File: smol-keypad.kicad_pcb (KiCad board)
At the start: 2 copper layers, 78.6 x 99.2 mm, 34 parts, among them SW1 SW_PUSH, U1 ProMicro

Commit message: test
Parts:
- moved D16 65.4 mm to (102.4, 127.0), turned to 0 degrees
- moved D4 64.0 mm to (159.5, 127.0), turned to 0 degrees
- moved MX13 58.7 mm to (102.4, 61.9), turned to 270 degrees
- moved MX1 57.2 mm to (159.5, 61.9), turned to 270 degrees
- moved MX16 57.2 mm to (102.4, 119.1), turned to 270 degrees
- moved MX4 55.6 mm to (159.5, 119.1), turned to 270 degrees
- moved D12 52.6 mm to (121.5, 127.0), turned to 0 degrees
- moved D8 52.0 mm to (140.5, 127.0), turned to 0 degrees
- moved D13 51.4 mm to (102.4, 69.8), turned to 0 degrees
- moved D1 49.6 mm to (159.5, 69.8), turned to 0 degrees
- moved D15 47.8 mm to (102.4, 108.0), turned to 0 degrees
- moved D3 45.8 mm to (159.5, 108.0), turned to 0 degrees
- moved MX14 44.0 mm to (102.4, 81.0), turned to 270 degrees
- moved MX9 44.0 mm to (121.4, 61.9), turned to 270 degrees
- moved MX15 43.3 mm to (102.4, 100.0), turned to 270 degrees
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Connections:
- U1 pad 10: Net-(U1-Pad10) -> /row1
- U1 pad 11: Net-(U1-Pad11) -> /row2
- U1 pad 12: Net-(U1-Pad12) -> /row3
- U1 pad 5: Net-(U1-Pad5) -> /col3
- U1 pad 6: Net-(U1-Pad6) -> /col2
- U1 pad 7: Net-(U1-Pad7) -> /col1
- U1 pad 8: Net-(U1-Pad8) -> /col0
- U1 pad 9: Net-(U1-Pad9) -> /row0
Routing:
- net /col3: track 57.1 -> 139.7 mm
- net /col2: track 57.1 -> 122.5 mm
- net /col1: track 57.1 -> 103.5 mm
- net /row3: track 58.8 -> 102.8 mm
- net GND: track 0.00 -> 40.7 mm
- net Net-(SW1-Pad1): track 0.00 -> 36.6 mm
- net /row0: track 58.8 -> 89.3 mm
- net /row2: track 58.9 -> 87.2 mm
- net /col0: track 57.1 -> 85.4 mm
- net /row1: track 58.8 -> 81.3 mm
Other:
- board size 78.6 x 99.2 mm -> 79.4 x 103.2 mm

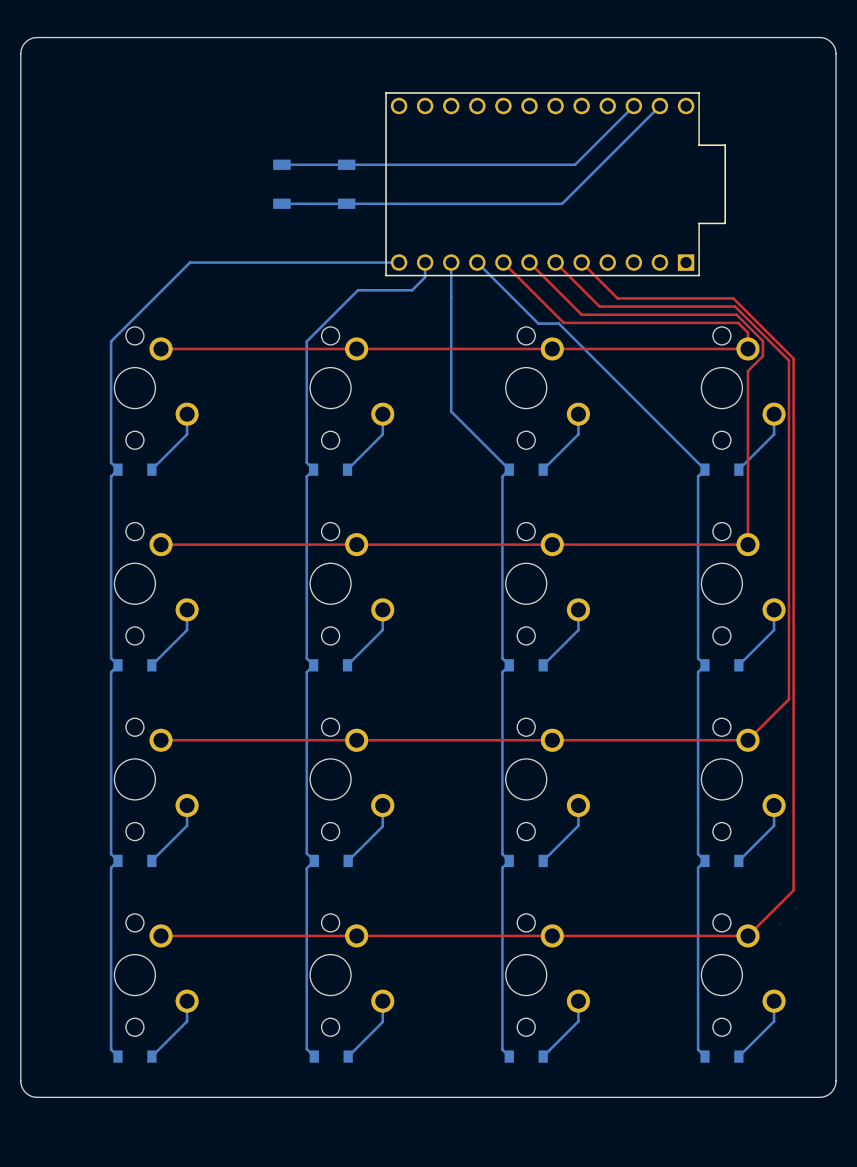
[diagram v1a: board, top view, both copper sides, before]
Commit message: remove submodules from project
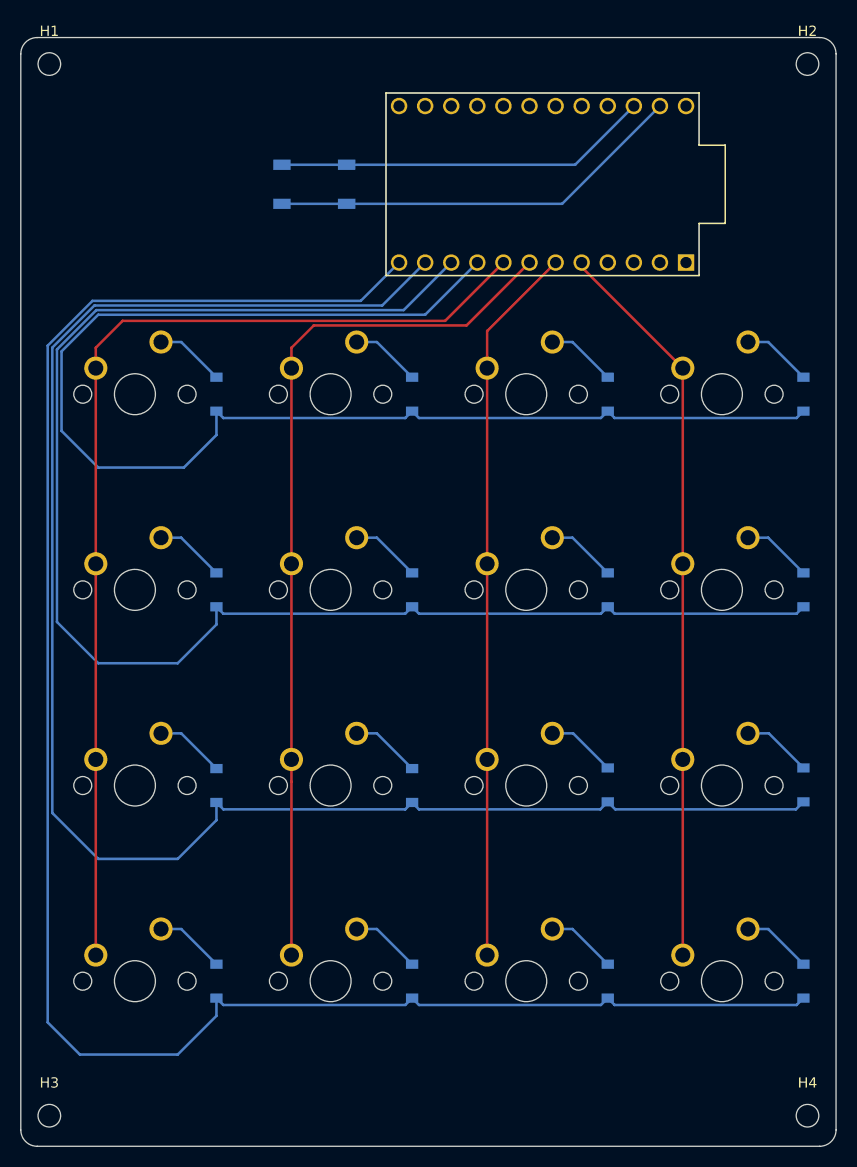
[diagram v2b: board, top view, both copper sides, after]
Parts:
- added H1: MountingHole, MountingHole:MountingHole_2.2mm_M2, F.Cu at (94.1, 30.4)
- added H2: MountingHole, MountingHole:MountingHole_2.2mm_M2, F.Cu at (167.9, 30.4)
- added H3: MountingHole, MountingHole:MountingHole_2.2mm_M2, F.Cu at (94.1, 132.8)
- added H4: MountingHole, MountingHole:MountingHole_2.2mm_M2, F.Cu at (167.9, 132.8)
- moved D16 65.5 mm to (167.5, 119.7), turned to 90 degrees
- moved D4 65.0 mm to (167.5, 62.5), turned to 90 degrees
- moved MX13 57.7 mm to (102.4, 119.7), turned to 0 degrees
- moved MX1 57.2 mm to (102.4, 62.5), turned to 0 degrees
- moved MX16 57.2 mm to (159.5, 119.7), turned to 0 degrees
- moved MX4 56.6 mm to (159.5, 62.5), turned to 0 degrees
- moved D12 53.0 mm to (167.5, 100.5), turned to 90 degrees
- moved D8 52.9 mm to (167.5, 81.6), turned to 90 degrees
- moved D13 50.4 mm to (110.3, 119.7), turned to 90 degrees
- moved D1 49.8 mm to (110.3, 62.5), turned to 90 degrees
- moved D15 47.5 mm to (148.4, 119.7), turned to 90 degrees
- moved D3 46.8 mm to (148.4, 62.5), turned to 90 degrees
- moved MX9 43.1 mm to (102.4, 100.6), turned to 0 degrees
- moved MX14 43.1 mm to (121.4, 119.7), turned to 0 degrees
- moved MX5 42.9 mm to (102.4, 81.6), turned to 0 degrees
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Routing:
- net /row3: track 102.8 -> 183.3 mm
- net /row2: track 87.2 -> 165.1 mm
- net /col3: track 139.7 -> 71.5 mm
- net /row1: track 81.3 -> 147.7 mm
- net /col2: track 122.5 -> 70.2 mm
- net /row0: track 89.3 -> 130.8 mm
- net /col1: track 103.5 -> 85.7 mm
- net /col0: track 85.4 -> 102.3 mm
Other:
- board size 79.4 x 103.2 mm -> 79.4 x 107.9 mm
